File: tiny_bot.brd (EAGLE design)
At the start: 100 x 80 mm, 33 parts, among them IC1 SN754410PDIP, U1 ATMEGA328P_PDIP, X1 16 MHz

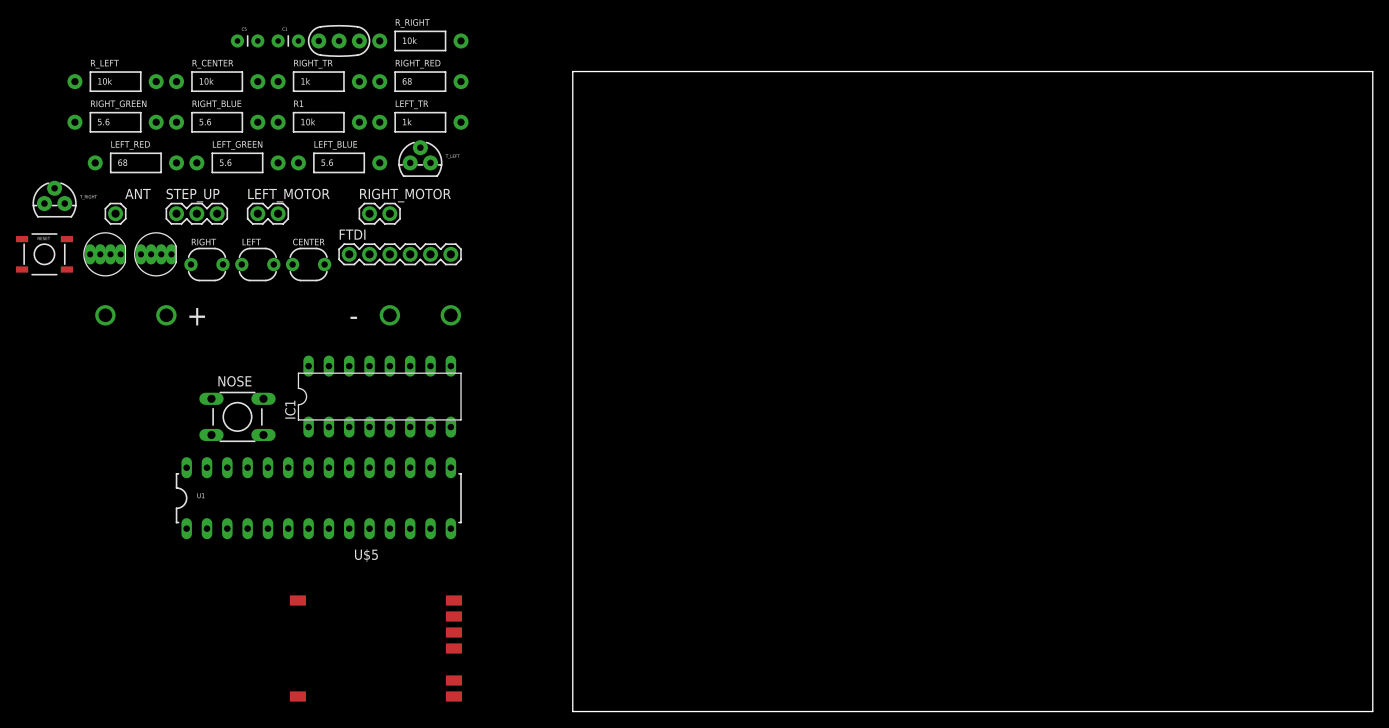
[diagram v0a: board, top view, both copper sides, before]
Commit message: Fixed LED problem; Started board layout
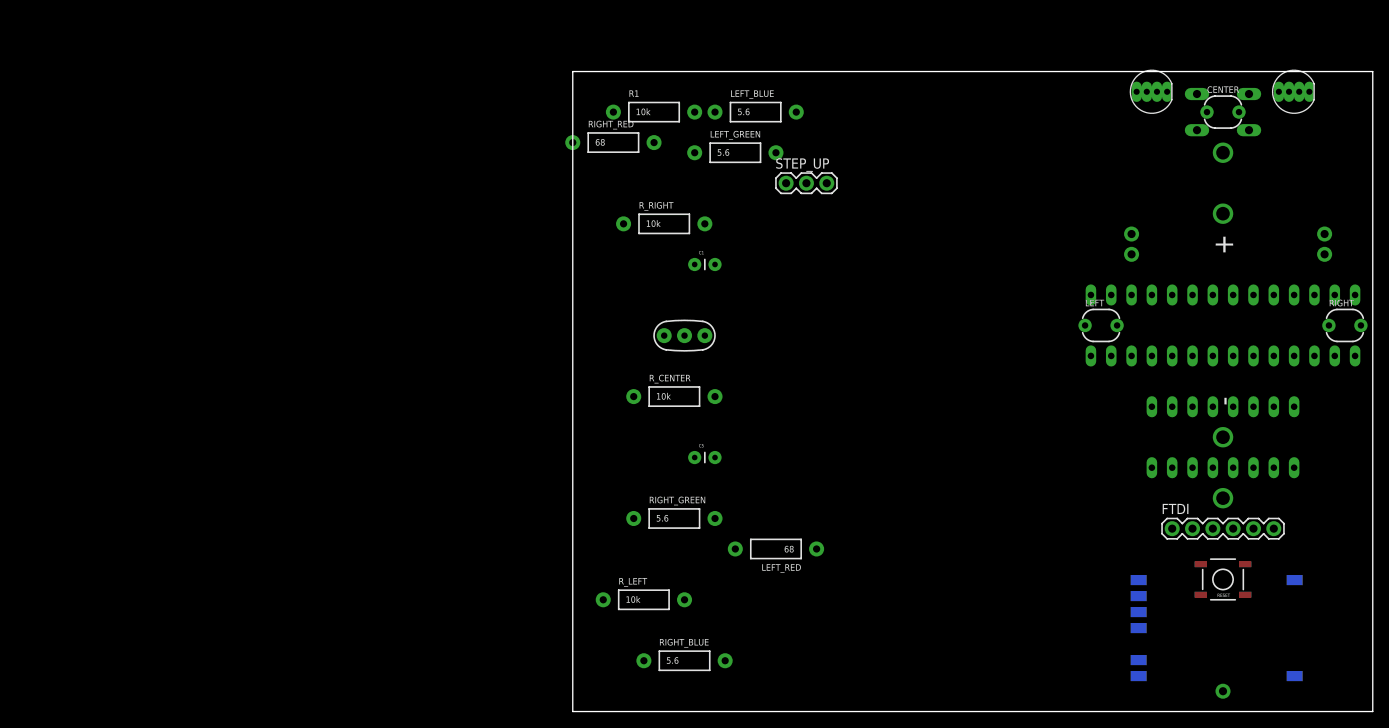
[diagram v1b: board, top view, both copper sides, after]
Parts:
- removed LEFT_TR, RIGHT_TR: 1k, SparkFun-Passives:AXIAL-0.4
- removed T_LEFT, T_RIGHT: (no value), SparkFun-DiscreteSemi:TO-92
- moved RESET 152.8 mm to (81.3, 16.5), turned to 180 degrees
- moved ANT 150.8 mm to (81.3, 2.54), flipped to the bottom
- moved RIGHT_EYE 150.0 mm to (90.2, 77.5)
- moved RIGHT 142.4 mm to (96.5, 48.3)
- moved NOSE 128.9 mm to (81.3, 74.9), flipped to the bottom
- moved LEFT_EYE 126.1 mm to (72.4, 77.5)
- moved RIGHT_MOTOR 119.5 mm to (94.0, 57.1), flipped to the bottom, turned to 90 degrees
- moved BATTERY 118.1 mm to (81.3, 48.3), turned to 270 degrees
- moved CENTER 115.9 mm to (81.3, 74.9)
- moved U1 115.1 mm to (81.3, 48.3), flipped to the bottom
- moved LEFT_MOTOR 109.2 mm to (69.8, 59.7), flipped to the bottom, turned to 270 degrees
- moved FTDI 108.4 mm to (74.9, 22.9)
- moved LEFT 105.7 mm to (66.0, 48.3)
- moved IC1 105.5 mm to (81.3, 34.3), flipped to the bottom
- moved U$5 101.6 mm to (78.7, 11.4), flipped to the bottom
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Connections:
- removed net D5: LEFT_TR.P$2
- removed net LEFT_DIR: RIGHT_TR.P$2
- removed net N$10: RIGHT_EYE.2, T_RIGHT.1
- removed net N$11: LEFT_TR.P$1, T_LEFT.2
- removed net N$12: RIGHT_TR.P$1, T_RIGHT.2
- removed net N$9: LEFT_EYE.2, T_LEFT.1
- removed net PWR: FTDI.3
- net GND: now also LEFT_EYE.2, RIGHT_EYE.2; no longer T_LEFT.3, T_RIGHT.3
